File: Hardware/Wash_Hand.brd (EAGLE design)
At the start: 71.1 x 48.3 mm, 91 parts, among them IC1 LM358D, IC2 LP298XS, IC3 405016TSSOP, J1 I2C, J2 ICSP, J3 SPI, J4 9V_CONN, J5 EXT_VCC, J6 6_PIN_SERIAL_CABLEPTH, J7 OP_B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

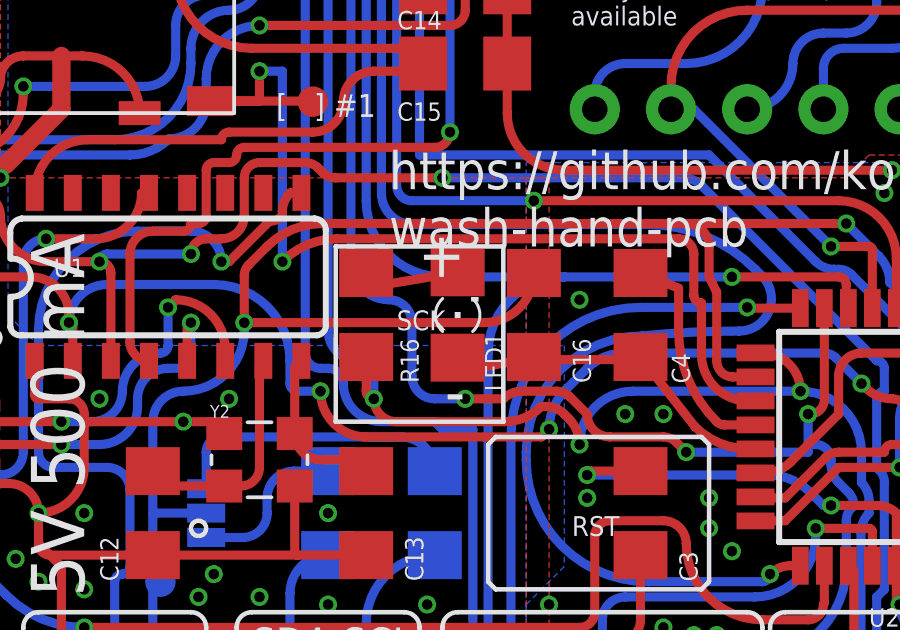
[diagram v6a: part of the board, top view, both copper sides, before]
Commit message: Board/Schematic: Re-orient LED1 to face correctly.
It was turned around.

Signed-off-by: Konrad Rzeszutek Wilk <konrad@kernel.org>
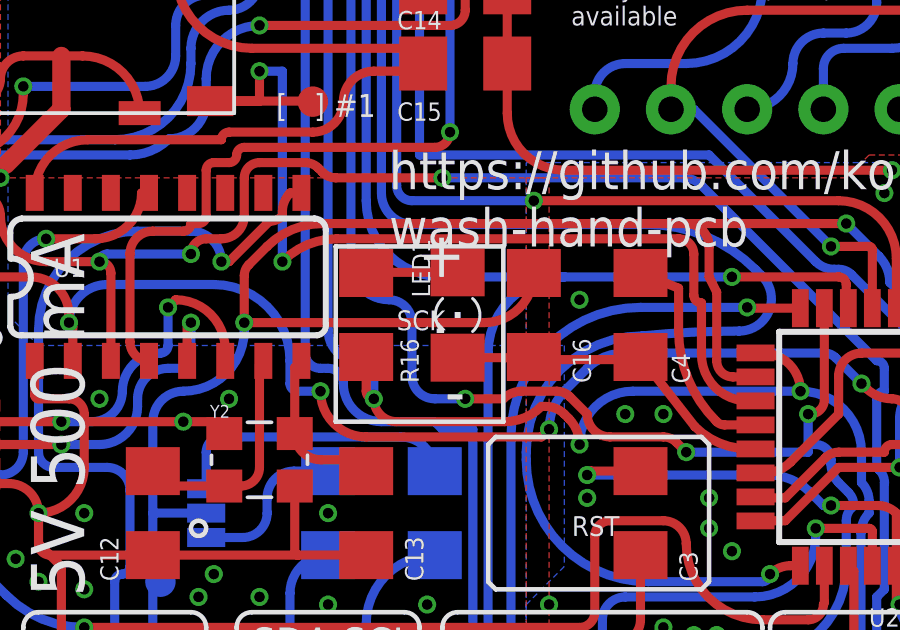
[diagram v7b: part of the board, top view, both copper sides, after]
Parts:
- turned LED1 to 270 degrees
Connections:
- net 0: now also LED1.C; no longer LED1.A
- net N$7: now also LED1.A; no longer LED1.C
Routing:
- net 0: track 370.3 -> 369.8 mm
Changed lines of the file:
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@@
 <element name="U$9" library="adafruit" library_urn="urn:adsk.eagle:library:420" package="FIDUCIAL_1MM" package3d_urn="urn:adsk.eagle:package:6240632/1" value="FIDUCIAL" x="2.54" y="39.116" smashed="yes"/>
 <element name="U$10" library="adafruit" library_urn="urn:adsk.eagle:library:420" package="FIDUCIAL_1MM" package3d_urn="urn:adsk.eagle:package:6240632/1" value="FIDUCIAL" x="1.524" y="7.366" smashed="yes"/>
-<element name="LED1" library="adafruit" library_urn="urn:adsk.eagle:library:420" package="1206" package3d_urn="urn:adsk.eagle:package:6240349/1" value="RED" x="21.336" y="17.018" smashed="yes" rot="R90">
-<attribute name="NAME" x="22.86" y="14.478" size="0.6096" layer="25" ratio="20" rot="R90"/>
-<attribute name="VALUE" x="22.86" y="17.78" size="0.6096" layer="27" ratio="14" rot="R90"/>
+<element name="LED1" library="adafruit" library_urn="urn:adsk.eagle:library:420" package="1206" package3d_urn="urn:adsk.eagle:package:6240349/1" value="RED" x="21.336" y="17.018" smashed="yes" rot="R270">
+<attribute name="NAME" x="19.812" y="19.558" size="0.6096" layer="25" ratio="20" rot="R270"/>
+<attribute name="VALUE" x="19.812" y="16.256" size="0.6096" layer="27" ratio="14" rot="R270"/>
 </element>
 <element name="R16" library="darnok_common" package="1206" value="1K" x="18.288" y="17.018" smashed="yes" rot="R270">
@@
 <via x="17.018" y="5.842" extent="1-16" drill="0.35"/>
 <via x="13.462" y="5.842" extent="1-16" drill="0.35"/>
-<contactref element="LED1" pad="A"/>
 <wire x1="62.354" y1="21.466" x2="62.992" y2="20.828" width="0.3048" layer="1" curve="-90"/>
 <contactref element="U1" pad="1"/>
@@
 <wire x1="9.768" y1="35.698" x2="7.62" y2="37.846" width="0.3048" layer="1" curve="-90"/>
 <contactref element="C16" pad="1"/>
-<wire x1="21.336" y1="15.596" x2="21.358" y2="15.11" width="0.3048" layer="1" curve="-90"/>
-<wire x1="21.358" y1="15.11" x2="23.876" y2="15.618" width="0.3048" layer="1"/>
 <wire x1="23.876" y1="15.618" x2="23.963009375" y2="15.530990625" width="0.3048" layer="1" curve="90"/>
 <wire x1="23.963009375" y1="15.530990625" x2="27.444096875" y2="15.530990625" width="0.3048" layer="1"/>
@@
 <wire x1="67.818" y1="11.43" x2="65.024" y2="11.43" width="0.3048" layer="1"/>
 <wire x1="65.024" y1="11.43" x2="64.77" y2="11.176" width="0.3048" layer="1" curve="90"/>
+<contactref element="LED1" pad="C"/>
+<wire x1="21.336" y1="15.596" x2="23.854" y2="15.596" width="0.3048" layer="1"/>
+<wire x1="23.854" y1="15.596" x2="23.876" y2="15.618" width="0.3048" layer="1"/>
 </signal>
 <signal name="D0">
@@
 <via x="47.244" y="45.72" extent="1-16" drill="0.35"/>
 </signal>
-<signal name="N$7">
-<contactref element="R16" pad="1"/>
-<contactref element="LED1" pad="C"/>
-<wire x1="21.336" y1="18.44" x2="18.31" y2="17.932" width="0.3048" layer="1"/>
-<wire x1="18.31" y1="17.932" x2="18.288" y2="18.418" width="0.3048" layer="1" curve="90"/>
-</signal>
 <signal name="CD">
 <contactref element="U2" pad="19"/>
@@
 <wire x1="66.424" y1="39.9766" x2="66.0146" y2="40.386" width="0.3048" layer="1" curve="90"/>
 </signal>
+<signal name="N$7">
+<contactref element="LED1" pad="A"/>
+<contactref element="R16" pad="1"/>
+<wire x1="21.336" y1="18.44" x2="18.31" y2="18.44" width="0.3048" layer="1"/>
+<wire x1="18.31" y1="18.44" x2="18.288" y2="18.418" width="0.3048" layer="1"/>
+</signal>
 </signals>
